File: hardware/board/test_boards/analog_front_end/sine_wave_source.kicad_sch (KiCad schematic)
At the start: 18 parts, among them U1 LTC6261, U7 AD9833xRM, U8 LTC6263, X1 ECS-TXO-2016

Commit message: add notes to pcb schematic for cleaner power supply layout to reduce spikes
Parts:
- U1: Manufacturer (none) -> Analog Devices Inc.; Manufacturer Number (none) -> LTC6261HS6#TRMPBF
- U8: Manufacturer (none) -> Analog Devices Inc.; Manufacturer Number (none) -> LTC6263IMS#PBF

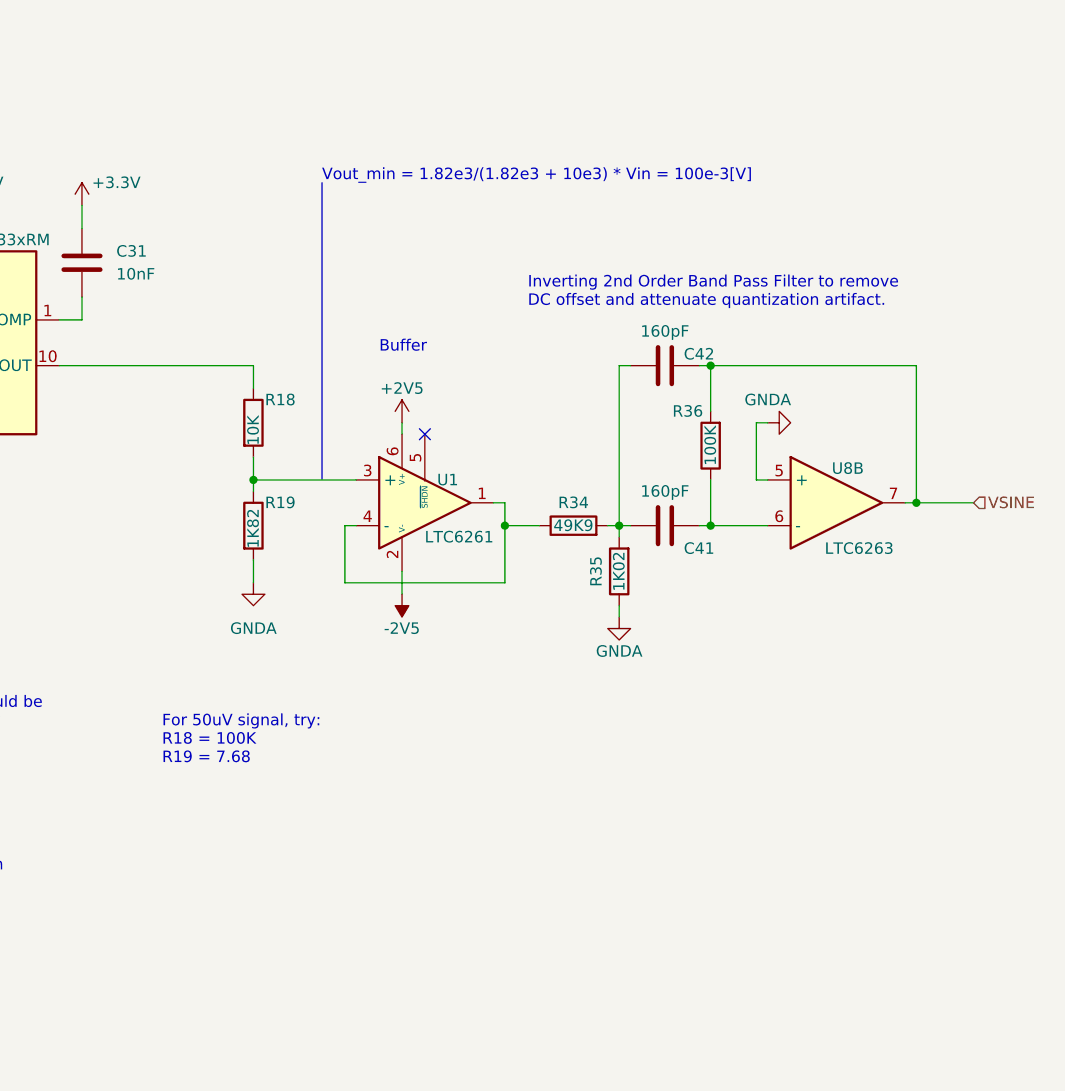
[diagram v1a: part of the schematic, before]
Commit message: pcb rev3 with pcb guard and cable shield guard option
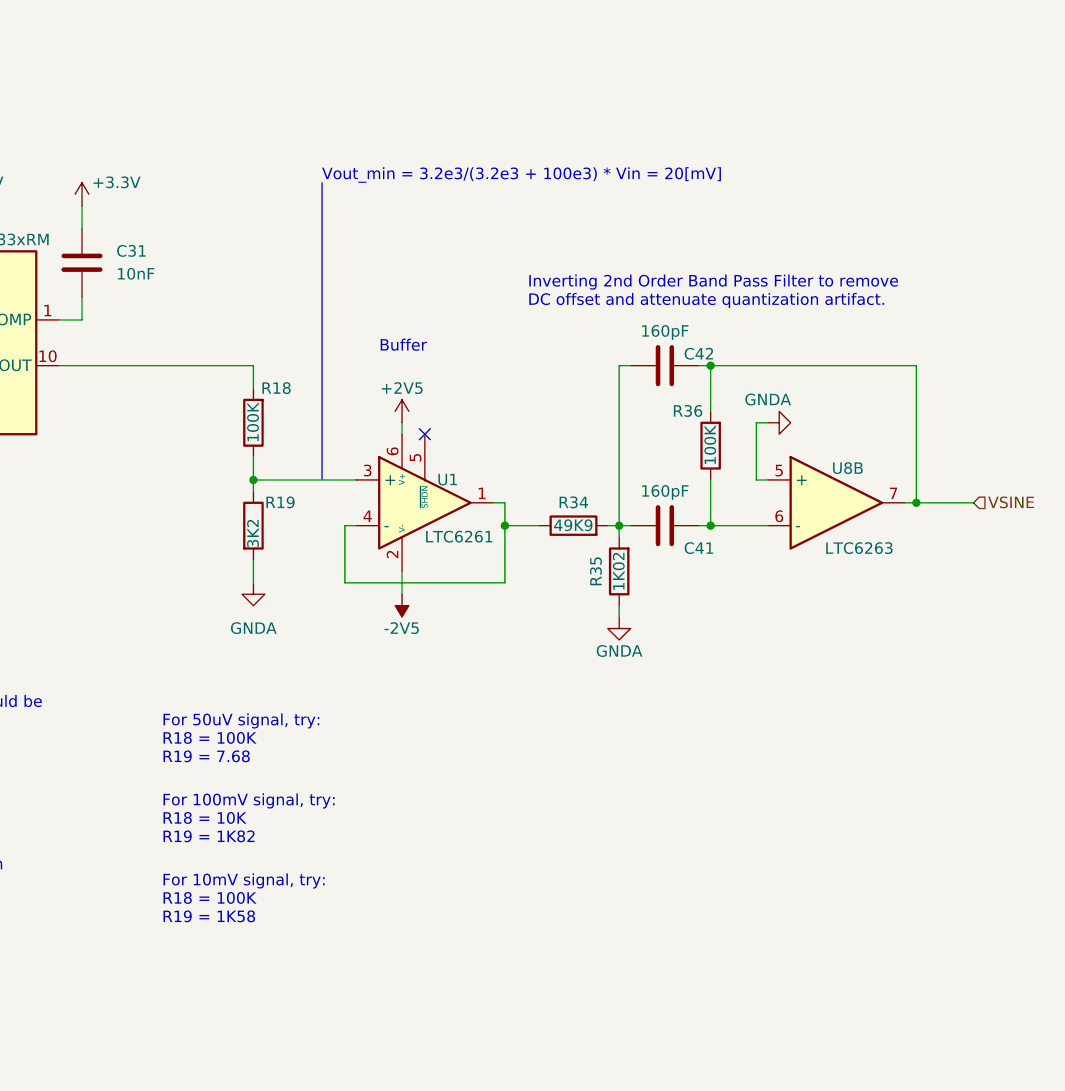
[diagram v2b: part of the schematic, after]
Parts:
- R18: value 10K -> 100K; footprint Resistor_SMD:R_0603_1608Metric_Pad0.98x0.95mm_HandSolder -> Resistor_SMD:R_0402_1005Metric_Pad0.72x0.64mm_HandSolder; Link https://www.digikey.com/en/products/detail/yageo/RT0603BRD1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 -> https://www.digikey.com/en/products/detail/yageo/RT0402BRD0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; Manufacturer Number RT0603BRD1010KL -> RT0402BRD07100KL
- R19: value 1K82 -> 3K2; footprint Resistor_SMD:R_0603_1608Metric_Pad0.98x0.95mm_HandSolder -> Resistor_SMD:R_0402_1005Metric_Pad0.72x0.64mm_HandSolder; Link https://www.digikey.com/en/products/detail/yageo/RT0603BRD0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 -> https://www.digikey.com/en/products/detail/yageo/RT0402BRD0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; Manufacturer Number RT0603BRD071K82L -> RT0402BRD073K2L
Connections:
- net at R18.1: now also R19.1, U1.3 (+); no longer U7.10 (VOUT)
- new net: R18.2, U7.10 (VOUT)
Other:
- note added: "For 100mV signal, try: R18 = 10K R19 = 1K82"
- note added: "For 10mV signal, try: R18 = 100K R19 = 1K58"
- note added: "Vout_min = 3.2e3/(3.2e3 + 100e3) * Vin = 20[mV]"
- note removed: "Vout_min = 1.82e3/(1.82e3 + 10e3) * Vin = 100e-3[V]"
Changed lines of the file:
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@@
+    (effects (font (size 1.27 1.27)) (justify left bottom))
+  )
+  (text "For 10mV signal, try: \nR18 = 100K\nR19 = 1K58" (at 162.56 157.48 0)
     (effects (font (size 1.27 1.27)) (justify left bottom))
   )
@@
     (effects (font (size 1.27 1.27)) (justify left bottom))
   )
+  (text "For 100mV signal, try: \nR18 = 10K\nR19 = 1K82" (at 162.56 148.59 0)
+    (effects (font (size 1.27 1.27)) (justify left bottom))
+  )
   (text "AD9833 outputs a 650[mV] signal with\na 325[mV] offset.\nRout = 200[Ohm]"
     (at 123.19 55.88 0)
     (effects (font (size 1.27 1.27)) (justify left bottom))
   )
-  (text "Vout_min = 1.82e3/(1.82e3 + 10e3) * Vin = 100e-3[V]"
-    (at 180.34 74.93 0)
+  (text "Vout_min = 3.2e3/(3.2e3 + 100e3) * Vin = 20[mV]" (at 180.34 74.93 0)
     (effects (font (size 1.27 1.27)) (justify left bottom))
   )
@@
   (hierarchical_label "PICO" (shape input) (at 119.38 90.17 180)
     (effects (font (size 1.27 1.27)) (justify right))
+  )
+  (symbol (lib_id "Device:R") (at 172.72 101.6 180) (unit 1)
+    (in_bom yes) (on_board yes)
+    (property "Reference" "R18" (id 0) (at 175.26 97.79 0))
+    (property "Value" "100K" (id 1) (at 172.72 101.6 90))
+    (property "Footprint" "Resistor_SMD:R_0402_1005Metric_Pad0.72x0.64mm_HandSolder" (id 2) (at 174.498 101.6 90)
+      (effects (font (size 1.27 1.27)) hide)
+    )
+    (property "Datasheet" "https://www.yageo.com/upload/media/product/productsearch/datasheet/rchip/PYu-RT_1-to-0.01_RoHS_L_15.pdf" (id 3) (at 172.72 101.6 0)
+      (effects (font (size 1.27 1.27)) hide)
+    )
+    (property "Link" "https://www.digikey.com/en/products/detail/yageo/RT0402BRD07100KL/1068989" (id 4) (at 172.72 101.6 0)
+      (effects (font (size 1.27 1.27)) hide)
+    )
+    (property "Manufacturer" "Yageo" (id 5) (at 172.72 101.6 0)
+      (effects (font (size 1.27 1.27)) hide)
+    )
+    (property "Manufacturer Number" "RT0402BRD07100KL" (id 6) (at 172.72 101.6 0)
+      (effects (font (size 1.27 1.27)) hide)
+    )
+    (property "Notes" "" (id 7) (at 172.72 101.6 0)
+      (effects (font (size 1.27 1.27)) hide)
+    )
+    (property "Tolerance" "0.1%" (id 8) (at 172.72 101.6 0)
+      (effects (font (size 1.27 1.27)) hide)
+    )
+    (pin "1")
+    (pin "2")
   )
   (symbol (lib_id "power:GNDA") (at 24.13 180.34 0) (unit 1)
@@
     (pin "2")
   )
-  (symbol (lib_id "Device:R") (at 172.72 101.6 0) (unit 1)
-    (in_bom yes) (on_board yes)
-    (property "Reference" "R18" (id 0) (at 173.99 99.06 0)
-      (effects (font (size 1.27 1.27)) (justify left))
-    )
-    (property "Value" "10K" (id 1) (at 172.72 104.14 90)
-      (effects (font (size 1.27 1.27)) (justify left))
-    )
-    (property "Footprint" "Resistor_SMD:R_0603_1608Metric_Pad0.98x0.95mm_HandSolder" (id 2) (at 170.942 101.6 90)
-      (effects (font (size 1.27 1.27)) hide)
-    )
-    (property "Datasheet" "https://www.yageo.com/upload/media/product/productsearch/datasheet/rchip/PYu-RT_1-to-0.01_RoHS_L_15.pdf" (id 3) (at 172.72 101.6 0)
-      (effects (font (size 1.27 1.27)) hide)
-    )
-    (property "Link" "https://www.digikey.com/en/products/detail/yageo/RT0603BRD1010KL/9370957" (id 4) (at 172.72 101.6 0)
-      (effects (font (size 1.27 1.27)) hide)
-    )
-    (property "Manufacturer" "Yageo" (id 5) (at 172.72 101.6 0)
-      (effects (font (size 1.27 1.27)) hide)
-    )
-    (property "Manufacturer Number" "RT0603BRD1010KL" (id 6) (at 172.72 101.6 0)
-      (effects (font (size 1.27 1.27)) hide)
-    )
-    (property "Tolerance" "0.1%" (id 7) (at 172.72 101.6 0)
-      (effects (font (size 1.27 1.27)) hide)
-    )
-    (pin "1")
-    (pin "2")
-  )
   (symbol (lib_id "Device:C") (at 24.13 173.99 180) (unit 1)
     (in_bom yes) (on_board yes)
@@
       (effects (font (size 1.27 1.27)) (justify left))
     )
-    (property "Value" "1K82" (id 1) (at 172.72 115.57 90)
-      (effects (font (size 1.27 1.27)) (justify left))
-    )
-    (property "Footprint" "Resistor_SMD:R_0603_1608Metric_Pad0.98x0.95mm_HandSolder" (id 2) (at 170.942 113.03 90)
+    (property "Value" "3K2" (id 1) (at 172.72 115.57 90)
+      (effects (font (size 1.27 1.27)) (justify left))
+    )
+    (property "Footprint" "Resistor_SMD:R_0402_1005Metric_Pad0.72x0.64mm_HandSolder" (id 2) (at 170.942 113.03 90)
       (effects (font (size 1.27 1.27)) hide)
     )
@@
       (effects (font (size 1.27 1.27)) hide)
     )
-    (property "Link" "https://www.digikey.com/en/products/detail/yageo/RT0603BRD071K82L/1072339" (id 4) (at 172.72 113.03 0)
+    (property "Link" "https://www.digikey.com/en/products/detail/yageo/RT0402BRD073K2L/5926126" (id 4) (at 172.72 113.03 0)
       (effects (font (size 1.27 1.27)) hide)
     )
@@
       (effects (font (size 1.27 1.27)) hide)
     )
-    (property "Manufacturer Number" "RT0603BRD071K82L" (id 6) (at 172.72 113.03 0)
-      (effects (font (size 1.27 1.27)) hide)
-    )
+    (property "Manufacturer Number" "RT0402BRD073K2L" (id 6) (at 172.72 113.03 0)
+      (effects (font (size 1.27 1.27)) hide)
+    )

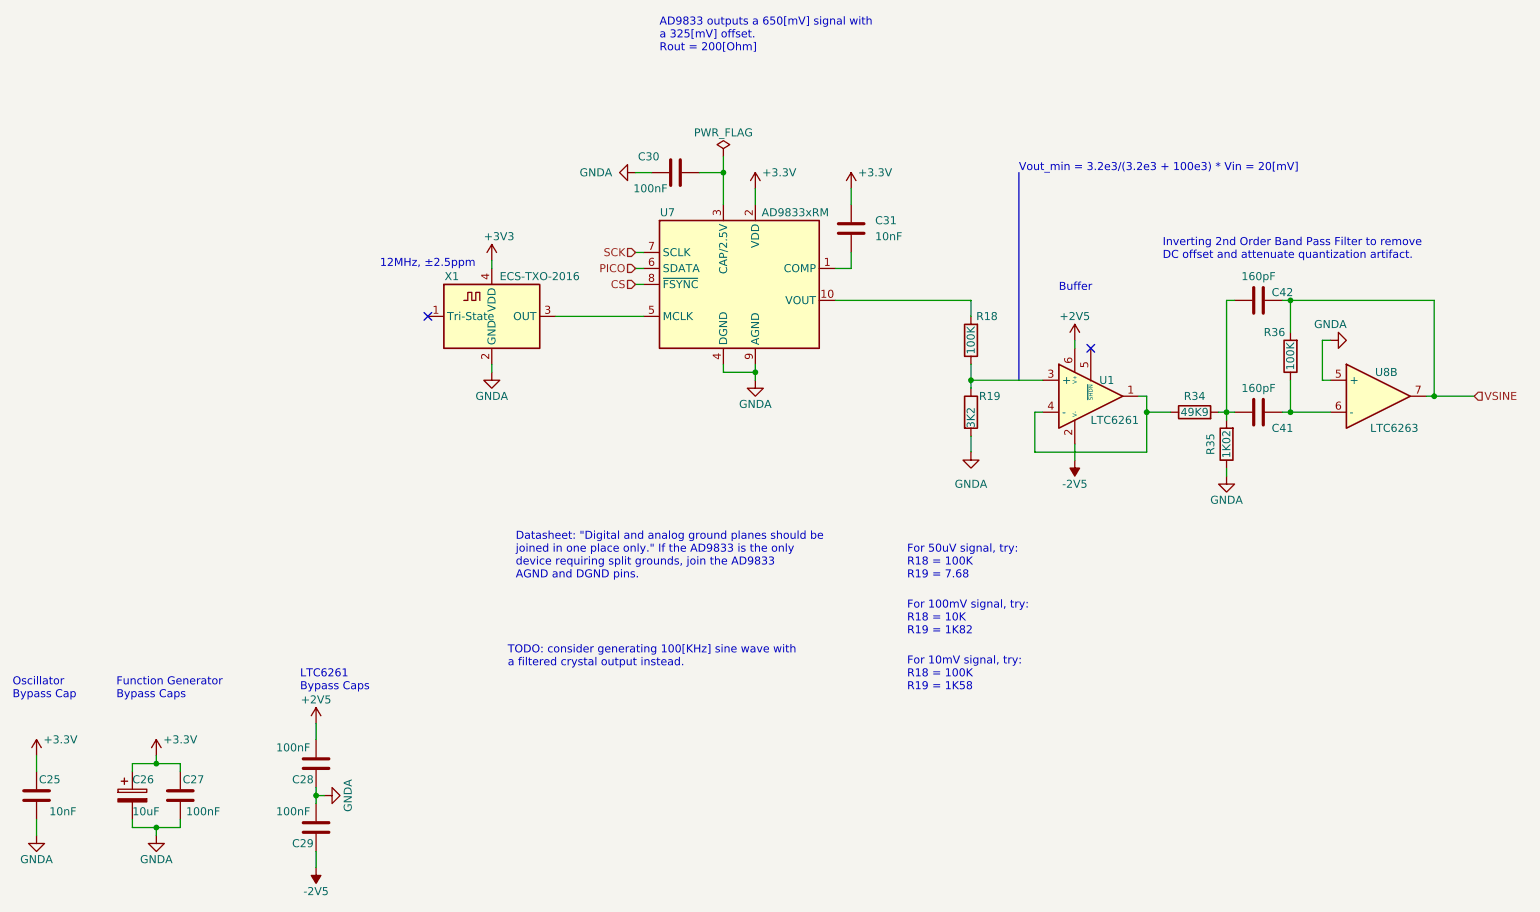
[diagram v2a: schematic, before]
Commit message: layout rev4 with triax and ltc6269
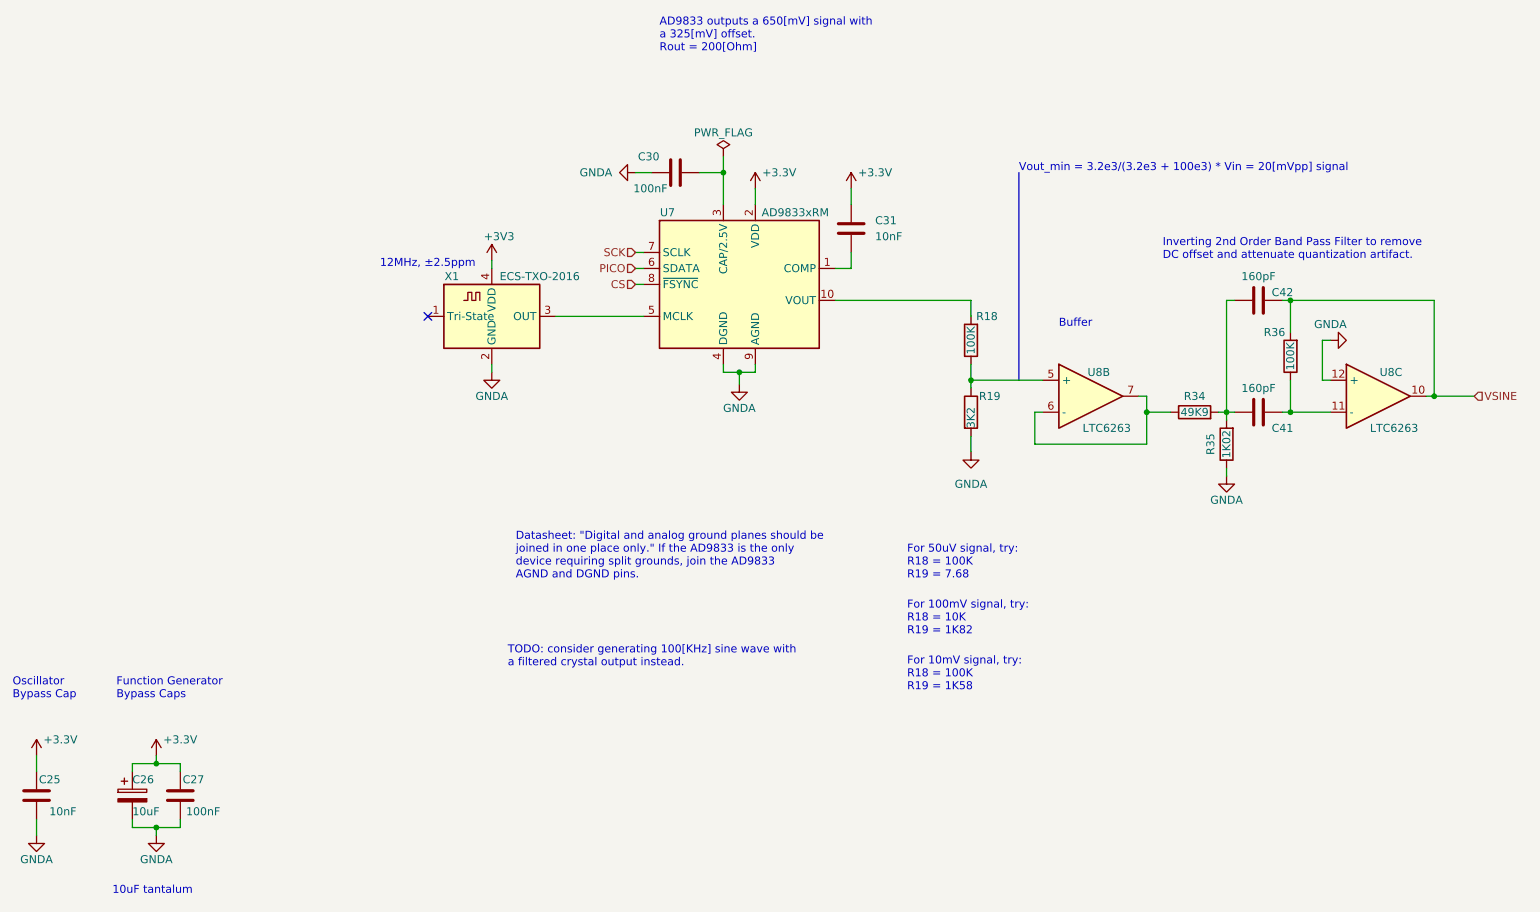
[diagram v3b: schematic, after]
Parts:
- removed C28, C29: 100nF, Capacitor_SMD:C_0402_1005Metric_Pad0.74x0.62mm_HandSolder, symbol Device:C
- removed U1: LTC6261, Package_TO_SOT_SMD:TSOT-23-6, symbol machine_agency_components:LTC6261
- added unit 3 of U8
- C26: footprint Capacitor_SMD:C_0603_1608Metric_Pad1.08x0.95mm_HandSolder -> Capacitor_SMD:C_0805_2012Metric_Pad1.18x1.45mm_HandSolder; Link https://www.digikey.com/en/products/detail/murata-electroni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 -> https://www.digikey.com/en/products/detail/kyocera-avx/F981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; Manufacturer Murata Electronics -> KYOCERA AVX; Manufacturer Number GRM188Z71A106MA73D -> F981C106MSAAS1; Rated Voltage 10V -> 16V; Temperature Coefficient X7R -> (none)
- U8: symbol machine_agency_components:LTC6263 -> kicad_component_library:LTC6263
- X1: symbol machine_agency_components:ECS-TXO-2016 -> kicad_component_library:ECS-TXO-2016
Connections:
- net GNDA: now also U8.12 (+); no longer U8.5 (+)
- net VSINE: now also U8.10; no longer U8.7
- net at R18.1, R19.1: now also U8.5 (+)
- net at C41.2, R36.1: now also U8.11 (-); no longer U8.6 (-)
- net at R34.1: now also U8.6 (-), U8.7
- no-connect marks 2 -> 1
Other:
- note added: "10uF tantalum"
- note added: "Vout_min = 3.2e3/(3.2e3 + 100e3) * Vin = 20[mVpp] signal"
- note removed: "LTC6261 Bypass Caps"
- note removed: "Vout_min = 3.2e3/(3.2e3 + 100e3) * Vin = 20[mV]"
- moved on the sheet: U8B

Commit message: update bom
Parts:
- C26: Link https://www.digikey.com/en/products/detail/kyocera-avx/F981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 -> https://www.digikey.com/en/products/detail/kemet/T529P106M0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; Manufacturer KYOCERA AVX -> Kemet; Manufacturer Number F981C106MSAAS1 -> T529P106M010AAE200; Notes (none) -> 200mOhm ESR @ 100KHz, marking on positive side; Rated Voltage 16V -> 10V
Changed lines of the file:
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@@
       (effects (font (size 1.27 1.27)) hide)
     )
-    (property "Datasheet" "https://datasheets.kyocera-avx.com/F98-AS1.pdf" (at 39.37 173.99 0)
+    (property "Datasheet" "https://connect.kemet.com:7667/gateway/IntelliData-ComponentDocumentation/1.0/download/specsheet/T529P106M010AAE200" (at 39.37 173.99 0)
       (effects (font (size 1.27 1.27)) hide)
     )
-    (property "Link" "https://www.digikey.com/en/products/detail/kyocera-avx/F981C106MSAAS1/4990380" (at 39.37 173.99 0)
+    (property "Link" "https://www.digikey.com/en/products/detail/kemet/T529P106M010AAE200/8582783" (at 39.37 173.99 0)
       (effects (font (size 1.27 1.27)) hide)
     )
-    (property "Manufacturer" "KYOCERA AVX" (at 39.37 173.99 0)
+    (property "Manufacturer" "Kemet" (at 39.37 173.99 0)
       (effects (font (size 1.27 1.27)) hide)
     )
-    (property "Manufacturer Number" "F981C106MSAAS1" (at 39.37 173.99 0)
+    (property "Manufacturer Number" "T529P106M010AAE200" (at 39.37 173.99 0)
       (effects (font (size 1.27 1.27)) hide)
     )
-    (property "Rated Voltage" "16V" (at 39.37 173.99 0)
+    (property "Rated Voltage" "10V" (at 39.37 173.99 0)
       (effects (font (size 1.27 1.27)) hide)
     )
@@
       (effects (font (size 1.27 1.27)) hide)
     )
+    (property "Notes" "200mOhm ESR @ 100KHz, marking on positive side" (at 39.37 173.99 0)
+      (effects (font (size 1.27 1.27)) hide)
+    )
